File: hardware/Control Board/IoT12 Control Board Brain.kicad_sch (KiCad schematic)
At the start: 44 parts, among them J10 USB_B_Micro, J11 Conn_ARM_JTAG_SWD_10, J9 Conn_ARM_JTAG_SWD_10, SW2 SW_Push, U1 ATSAMD21G18A-AU, U6 AT24C32, Y1 32768Hz

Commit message: Start of next iteration.
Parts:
- removed C1, C2: 6.8pF, Capacitor_SMD:C_0805_2012Metric_Pad1.18x1.45mm_HandSolder, symbol Device:C
- removed C35, C36, C37, C38: 100nF, Capacitor_SMD:C_0805_2012Metric_Pad1.18x1.45mm_HandSolder, symbol Device:C
- removed C40, C41: 1uF, Capacitor_SMD:C_0805_2012Metric_Pad1.18x1.45mm_HandSolder, symbol Device:C
- removed C50, C60, C61: 10uF, Capacitor_SMD:C_0805_2012Metric_Pad1.18x1.45mm_HandSolder, symbol Device:C
- removed D10: Amber, LED_SMD:LED_0805_2012Metric_Pad1.15x1.40mm_HandSolder, symbol Device:LED
- removed D3, D4: BAV99, Package_TO_SOT_SMD:SOT-23, symbol Diode:BAV99
- removed J10: USB_B_Micro, Connector_USB-fixed:USB_Micro-B_Amphenol_10118194_Horizontal, symbol Connector:USB_B_Micro
- removed J11, J9: Conn_ARM_JTAG_SWD_10, Connector_PinHeader_2.54mm:PinHeader_2x05_P2.54mm_Vertical, symbol Connector:Conn_ARM_JTAG_SWD_10
- removed L2: 10uH, Inductor_SMD:L_0805_2012Metric_Pad1.15x1.40mm_HandSolder, symbol Device:L_Small
- removed R20: 470R, Resistor_SMD:R_0805_2012Metric_Pad1.20x1.40mm_HandSolder, symbol Device:R
- removed R53, R54, R57: 4k7, Resistor_SMD:R_0805_2012Metric_Pad1.20x1.40mm_HandSolder, symbol Device:R
- removed SW2: SW_Push, Button_Switch_SMD:SW_SPST_CK_RS282G05A3, symbol Switch:SW_Push
- removed TP1, TP10, TP11, TP12, TP13, TP14, TP2, TP3, TP4, TP5, TP6, TP7, TP8, TP9: TestPoint, TestPoint-extra:TestPoint_Pad_D0.75mm, symbol Connector:TestPoint
- removed U1: ATSAMD21G18A-AU, Package_QFP:TQFP-48_7x7mm_P0.5mm, symbol MCU_Microchip_SAMD-extra:SAMD21G_ARDUINO_M0
- removed U6: AT24C32, Package_SO:SOIC-8_3.9x4.9mm_P1.27mm, symbol Memory_EEPROM:24LC32
- removed Y1: 32768Hz, Crystal:Crystal_C26-LF_D2.1mm_L6.5mm_Horizontal_1EP_style1, symbol Device:Crystal_GND3
- added A3: SAMD21_breakout, Module-extra:SAMD21_breakout, symbol MCU_Module-extra:SAMD21_breakout
- added C33: 100nF, Capacitor_SMD:C_0805_2012Metric_Pad1.18x1.45mm_HandSolder, symbol Device:C
- added C61: 100uF/35V, Capacitor_SMD:CP_Elec_6.3x7.7, symbol Device:C_Polarized
- added R41, R42: 4k7, Resistor_SMD:R_0805_2012Metric_Pad1.20x1.40mm_HandSolder, symbol Device:R
- added R77, R78: 100k, Resistor_SMD:R_0805_2012Metric_Pad1.20x1.40mm_HandSolder, symbol Device:R
- added U1: W25Q64FVSSIG, Package_SO-fixed:SOIC-8_5.23x5.23mm_P1.27mm, symbol Memory_Flash-extra:W25Q64FV
- renumbered C73 to C60, R55 to R43, R56 to R44
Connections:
- net ROT_SW is gone; now on net I2S_SD: A1.8 (XTAL32K/IO33)
- net +5V: now also A3.28 (5V_I), C61.1
- net ADC_RDY: now also A3.8 (PA06/~D8)
- net ESP32_SCL: now also A3.12 (PA09/~D3/SCL2)
- net ESP32_SDA: now also A3.11 (PA08/~D2/SDA2)
- net GND: now also A3.25 (GND), A3.29 (GND), C33.2, C61.2, R78.1, U1.4 (GND)
- net HEAT_INT: now also A3.13 (PA14/~D4)
- net HEAT_PWM: now also A3.10 (PA18/~D10)
- net HEAT_SCL: now also A3.21 (PA23/SCL)
- net HEAT_SDA: now also A3.20 (PA22/SDA)
- net I2S_GAIN0: now also A1.15 (IO13/TCK)
- net I2S_GAIN1: now also A1.12 (IO14/TMS)
- net IRON_CURRENT: now also A3.7 (PB02/A5)
- net NTC: now also A3.2 (PA02/DAC/A0)
- net TEMP: now also A3.3 (PB08/A1)
- net VIN: now also A3.6 (PA05/A4)
- net TFT_~{CS}: now reaches A1.23 (IO15/TDO/BH)
- net TFT_MISO: now reaches A1.31 (SPI_MISO/IO19)
- net TOUCH_~{IRQ}: now reaches A1.5 (IO34)
- net +3V3 renamed +3.3V
- net +3.3V: now also A3.26 (3V3_O), C33.1, R41.2, R42.2, R77.2, U1.3 (~{WP}/IO2), U1.7 (~{HOLD}/IO3), U1.8 (VCC)
- net LCD_CLK renamed TFT_SCLK
- net LCD_DATA-~{CMD} renamed TFT_~{RST}
- net LCD_DIN renamed TFT_MOSI
- net LCD_LED renamed TFT_LED
- net LCD_~{CE} renamed TOUCH_~{CS}
- net LCD_~{RST} renamed TFT_D~{C}
- net ROT_A: no longer names the net of A1.27 (RXD2/IO16)
- net ROT_B: no longer names the net of A1.28 (TXD2/IO17)
- new net 24V_ON: A3.9 (PA07/~D9)
- new net EXP_D5: A3.14 (PA15/~D5)
- new net EXP_D7: A3.16 (PA21/D7)
- new net EXP_SCL: A3.31 (PA17/~D13/SCL3/LED), R42.1
- new net EXP_SDA: A3.32 (PA16/~D11/SDA3), R41.1
- new net FLASH_~{CS}: A3.15 (PA20/~D6), R77.1, U1.1 (~{CS})
- new net MISO: A3.19 (PA12/MISO), U1.2 (DO/IO1)
- new net MOSI: A3.17 (PB10/MOSI), U1.5 (DI/IO0)
- new net SAMD21_~{RESET}: A3.24 (RESET)
- new net SCK: A3.18 (PB11/SCK), R78.2, U1.6 (CLK)
- new net SHAKE: A3.4 (PB09/A2), A3.5 (PA04/A3)
- no-connect marks 23 -> 18
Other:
- note added: "Memory"
- note removed: "Debug LED"
- note removed: "EEPROM"
- note removed: "Heat controller SWD"
- note removed: "Heat controller reset"
- note removed: "I2C: 0x50"
- company: (none) -> https://github.com/atoomnetmarc/IoT12
- title: IoT12-hardware brain -> IoT12 Control Board
- moved on the sheet: A1, C60, R43, R44

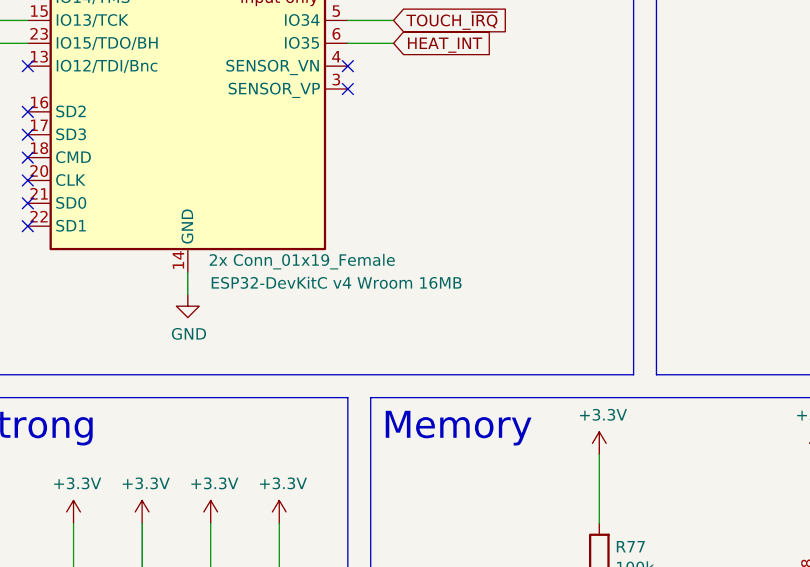
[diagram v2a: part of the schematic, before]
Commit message: Clarify use of ESP32-WROOM-32E.
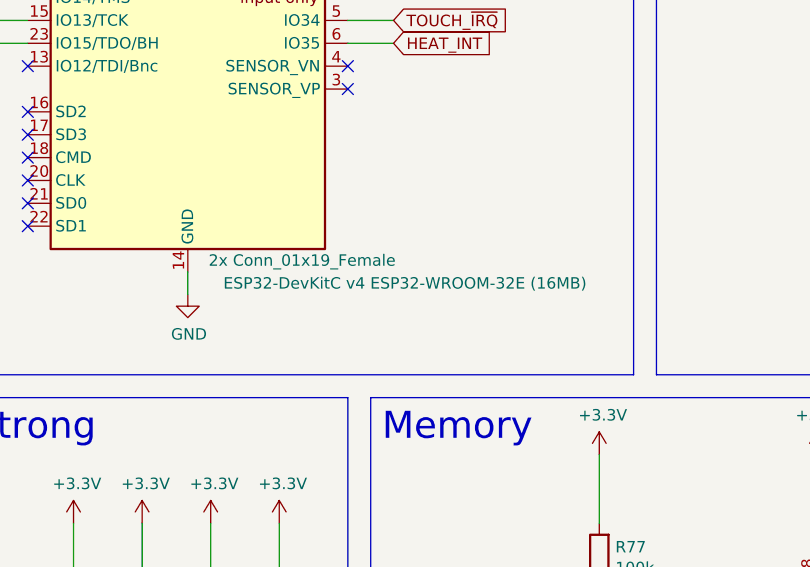
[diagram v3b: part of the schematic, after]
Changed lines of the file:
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@@
       (effects (font (size 1.27 1.27)) hide)
     )
-    (property "Description" "ESP32-DevKitC v4 Wroom 16MB" (at 77.47 121.92 0)
+    (property "Description" "ESP32-DevKitC v4 ESP32-WROOM-32E (16MB)" (at 85.09 121.92 0)
       (effects (font (size 1.27 1.27)))
     )
